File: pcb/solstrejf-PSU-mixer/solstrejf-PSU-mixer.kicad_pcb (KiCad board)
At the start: 2 copper layers, 114.9 x 54 mm, 43 parts, among them J1 LEFT JACK, J2 RIGHT JACK, J3 Conn_02x05_Odd_Even, J4 Conn_02x05_Odd_Even, J5 Conn_02x05_Odd_Even, J6 Conn_02x05_Odd_Even, J7 Transformer_Terminals, U1 TL072, U2 L7815, U3 L7915

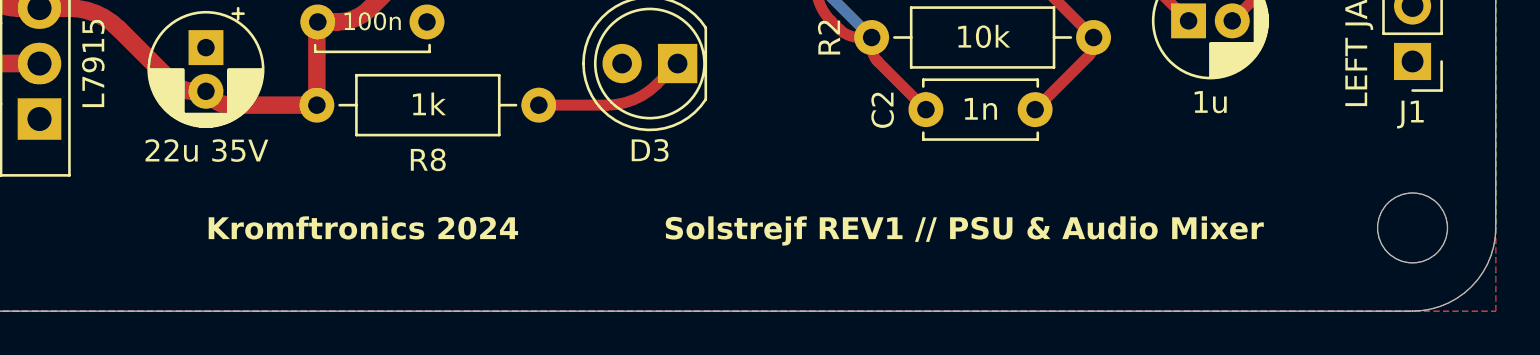
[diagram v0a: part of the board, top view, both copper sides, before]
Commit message: Added variable revision and date silkscreen prints for all four boards of Solstrejf
This means that the revision and issue date that is set in the page setup
of the PCB's will be update on the silscreen automatically so I don't forget
to update the revsions on the silkscreen :')
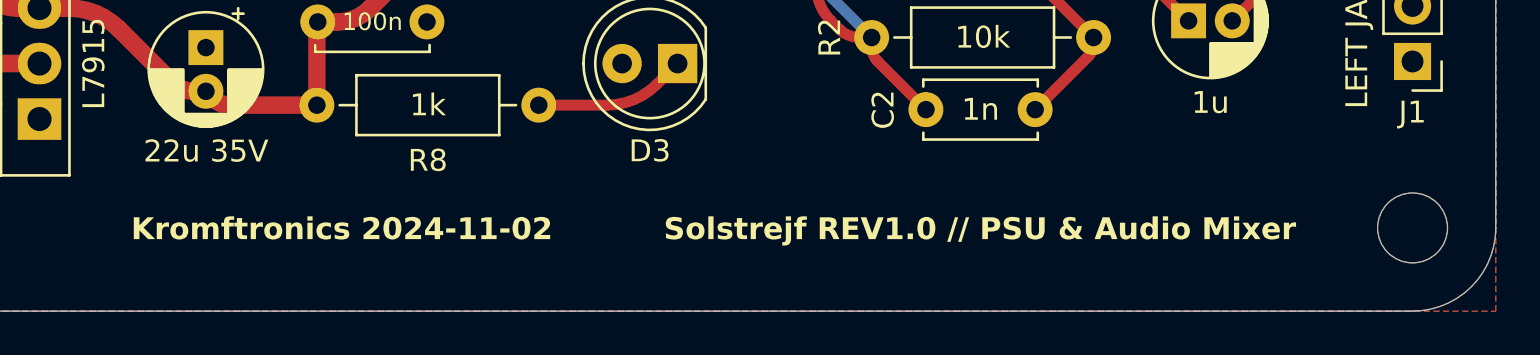
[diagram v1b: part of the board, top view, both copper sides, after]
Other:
- board text added: "${COMPANY} ${ISSUE_DATE}"
- board text added: "Solstrejf REV${REVISION} // PSU & Audio Mixer"
- board text removed: "Kromftronics 2024"
- board text removed: "Solstrejf REV1 // PSU & Audio Mixer"
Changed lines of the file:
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@@
 		(date "2024-11-02")
 		(rev "1.0")
+		(company "Kromftronics")
 	)
 	(layers
@@
 		)
 	)
-	(gr_text "Solstrejf REV1 // PSU & Audio Mixer"
+	(gr_text "Solstrejf REV${REVISION} // PSU & Audio Mixer"
 		(at 146.05 100.965 0)
 		(layer "F.SilkS")
@@
 		)
 	)
-	(gr_text "Kromftronics 2024"
-		(at 125.095 100.965 0)
+	(gr_text "${COMPANY} ${ISSUE_DATE}"
+		(at 121.666 100.965 0)
 		(layer "F.SilkS")
 		(effects
